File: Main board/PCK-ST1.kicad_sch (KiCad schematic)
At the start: 21 parts

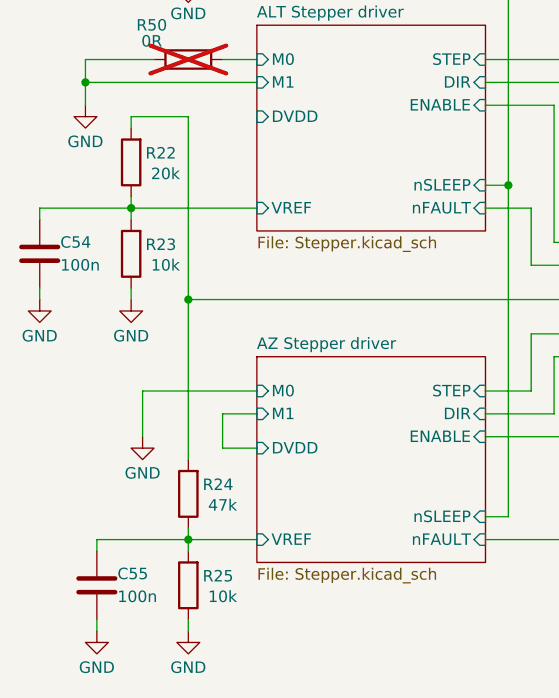
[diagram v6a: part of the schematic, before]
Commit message: Updated V1.0 schematic values
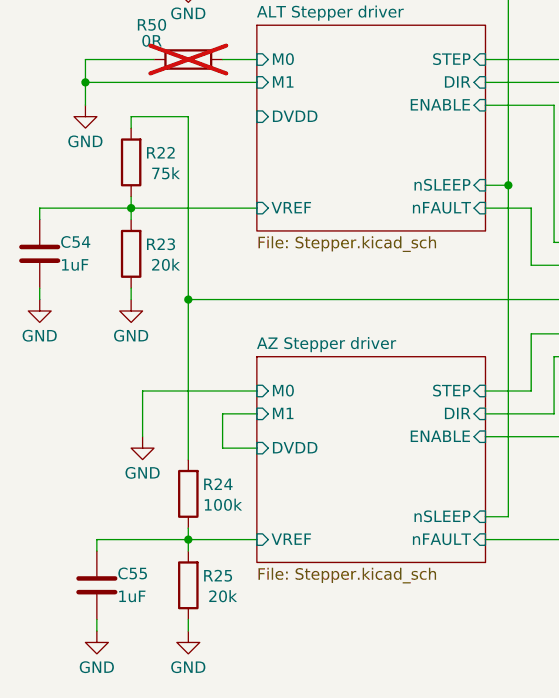
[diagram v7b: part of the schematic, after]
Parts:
- C54, C55: value 100n -> 1uF
- R22: value 20k -> 75k
- R23, R25: value 10k -> 20k
- R24: value 47k -> 100k
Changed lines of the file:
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@@
 			)
 		)
-		(property "Value" "10k"
+		(property "Value" "20k"
 			(at 82.55 133.35 0)
 			(effects
@@
 			)
 		)
-		(property "Value" "100n"
+		(property "Value" "1uF"
 			(at 70.866 133.35 0)
 			(effects
@@
 			)
 		)
-		(property "Value" "20k"
+		(property "Value" "75k"
 			(at 82.55 123.19 0)
 			(effects
@@
 			)
 		)
-		(property "Value" "100n"
+		(property "Value" "1uF"
 			(at 77.216 170.18 0)
 			(effects
@@
 			)
 		)
-		(property "Value" "10k"
+		(property "Value" "20k"
 			(at 88.9 170.18 0)
 			(effects
@@
 			)
 		)
-		(property "Value" "47k"
+		(property "Value" "100k"
 			(at 88.9 160.02 0)
 			(effects
